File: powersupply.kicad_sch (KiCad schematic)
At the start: 24 parts, among them SW1 SW_SPST, U3 MP28167GQ, U4 1047

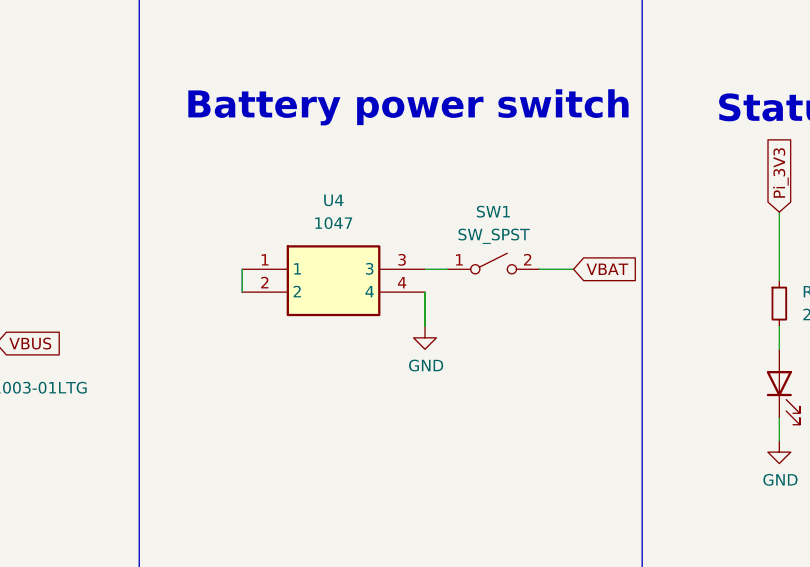
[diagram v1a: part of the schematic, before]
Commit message: Replace the switch with the real one: 633-CS12ANW03
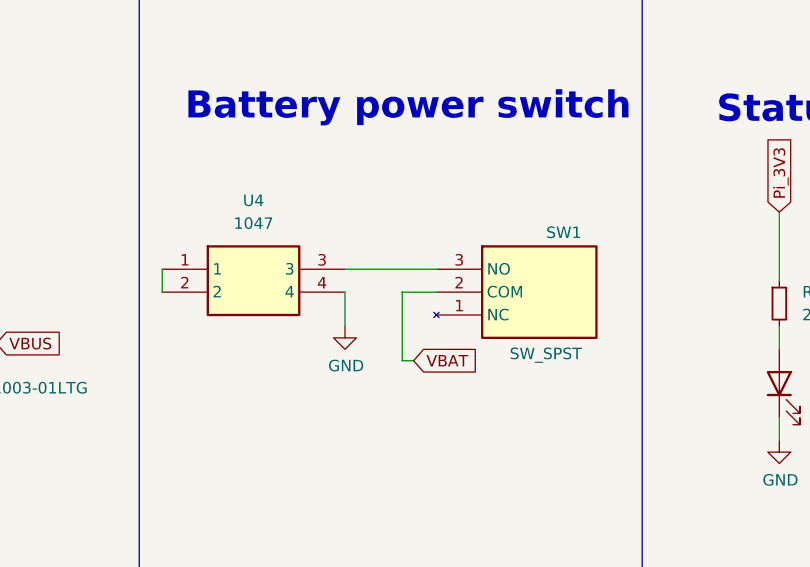
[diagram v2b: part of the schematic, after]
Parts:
- SW1: footprint Button_Switch_THT:SW_DIP_SPSTx01_Slide_9.78x4.72mm_W7.62mm_P2.54mm -> CS12ANW03; symbol Switch:SW_SPST -> STS1_EEE_lib:CS12ANW03; Height (none) -> 13.6; Manufacturer_Name (none) -> NKK Switches; Manufacturer_Part_Number (none) -> CS12ANW03; Mouser Part Number (none) -> 633-CS12ANW03; Mouser Price/Stock (none) -> https://www.mouser.co.uk/ProductDetail/NKK-Switches/CS12ANW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
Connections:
- net at SW1.1 (NC): no longer U4.3
- new net: SW1.3 (NO), U4.3
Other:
- moved on the sheet: U4
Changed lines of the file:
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@@
 	(wire
 		(pts
-			(xy 293.37 48.26) (xy 293.37 52.07)
+			(xy 284.48 48.26) (xy 284.48 52.07)
 		)
 		(stroke
@@
 	(wire
 		(pts
-			(xy 293.37 45.72) (xy 295.91 45.72)
+			(xy 284.48 45.72) (xy 294.64 45.72)
 		)
 		(stroke
@@
 	(wire
 		(pts
+			(xy 290.83 48.26) (xy 290.83 55.88)
+		)
+		(stroke
+			(width 0)
+			(type default)
+		)
+	)
+	(wire
+		(pts
 			(xy 344.17 39.37) (xy 344.17 46.99)
 		)
@@
 	(wire
 		(pts
-			(xy 273.05 45.72) (xy 273.05 48.26)
+			(xy 264.16 45.72) (xy 264.16 48.26)
 		)
 		(stroke
@@
 	(wire
 		(pts
-			(xy 306.07 45.72) (xy 309.88 45.72)
+			(xy 294.64 48.26) (xy 290.83 48.26)
 		)
 		(stroke
@@
 	(wire
 		(pts
+			(xy 290.83 55.88) (xy 292.1 55.88)
+		)
+		(stroke
+			(width 0)
+			(type default)
+		)
+	)
+	(wire
+		(pts
 			(xy 240.665 62.865) (xy 240.665 61.595)
 		)
@@
 	(global_label "VBAT"
 		(shape input)
-		(at 309.88 45.72 0)
+		(at 292.1 55.88 0)
 		(fields_autoplaced yes)
 		(effects
@@
 		)
 		(property "Intersheetrefs" "${INTERSHEET_REFS}"
-			(at 316.6258 45.72 0)
+			(at 298.8458 55.88 0)
 			(hide yes)
 			(show_name no)
@@
 	)
 	(symbol
-		(lib_id "Switch:SW_SPST")
-		(at 300.99 45.72 0)
+		(lib_id "STS1_EEE_lib:CS12ANW03")
+		(at 294.64 45.72 0)
 		(unit 1)
 		(body_style 1)
@@
 		(in_pos_files yes)
 		(dnp no)
-		(fields_autoplaced yes)
 		(property "Reference" "SW1"
-			(at 300.99 39.37 0)
+			(at 306.832 41.656 0)
 			(show_name no)
 			(do_not_autoplace no)
@@
 					(size 1.27 1.27)
 				)
+				(justify left)
 			)
 		)
 		(property "Value" "SW_SPST"
-			(at 300.99 41.91 0)
+			(at 302.768 55.118 0)
 			(show_name no)
 			(do_not_autoplace no)
@@
 					(size 1.27 1.27)
 				)
+				(justify left)
 			)
 		)
-		(property "Footprint" "Button_Switch_THT:SW_DIP_SPSTx01_Slide_9.78x4.72mm_W7.62mm_P2.54mm"
-			(at 300.99 45.72 0)
+		(property "Footprint" "CS12ANW03"
+			(at 313.69 140.64 0)
 			(hide yes)
 			(show_name no)
@@
 					(size 1.27 1.27)
 				)
+				(justify left top)
 			)
 		)
-		(property "Datasheet" ""
-			(at 300.99 45.72 0)
+		(property "Datasheet" "https://www.nkkswitches.com.hk/products/Slides/Slides%20CS/CS12ANW03/"
+			(at 313.69 240.64 0)
+			(hide yes)
+			(show_name no)
+			(do_not_autoplace no)
+			(effects
+				(font
+					(size 1.27 1.27)
+				)
+				(justify left top)
+			)
+		)
+		(property "Description" "NKK SWITCHES - CS12ANW03 - SWITCH, SLIDE, SPDT, 3A, 250V, TH"
+			(at 294.64 45.72 0)
+			(hide yes)
+			(show_name no)
+			(do_not_autoplace no)
+			(effects
+				(font
+					(size 1.27 1.27)
+				)
+			)
+		)
+		(property "Height" "13.6"
+			(at 313.69 440.64 0)
 			(hide yes)
 			(show_name no)
@@
 					(size 1.27 1.27)
 				)
+				(justify left top)
 			)
 		)
-		(property "Description" "Single Pole Single Throw (SPST) switch"
-			(at 300.99 45.72 0)
+		(property "Mouser Part Number" "633-CS12ANW03"
+			(at 313.69 540.64 0)
 			(hide yes)
 			(show_name no)
@@
 					(size 1.27 1.27)
 				)
+				(justify left top)
+			)
+		)
+		(property "Mouser Price/Stock" "https://www.mouser.co.uk/ProductDetail/NKK-Switches/CS12ANW03?qs=4P1McwaGddbVHu%252BBZT0egw%3D%3D"
+			(at 313.69 640.64 0)
+			(hide yes)
+			(show_name no)
+			(do_not_autoplace no)
+			(effects
+				(font
+					(size 1.27 1.27)
+				)
+				(justify left top)
+			)
+		)
+		(property "Manufacturer_Name" "NKK Switches"
+			(at 313.69 740.64 0)
+			(hide yes)
+			(show_name no)
+			(do_not_autoplace no)
+			(effects
+				(font
+					(size 1.27 1.27)
+				)
+				(justify left top)
+			)
+		)
+		(property "Manufacturer_Part_Number" "CS12ANW03"
+			(at 313.69 840.64 0)
+			(hide yes)
+			(show_name no)
+			(do_not_autoplace no)
+			(effects
+				(font
+					(size 1.27 1.27)
+				)
+				(justify left top)
 			)
 		)
@@
 		(pin "1"
 		)
+		(pin "3"
+		)
 		(instances
 			(project "STS1_EEE"
@@
 	(symbol
 		(lib_id "power:GND")
-		(at 293.37 52.07 0)
+		(at 284.48 52.07 0)
 		(unit 1)
 		(body_style 1)
@@
 		(dnp no)
 		(property "Reference" "#PWR047"
-			(at 293.37 58.42 0)
+			(at 284.48 58.42 0)
 			(hide yes)
 			(show_name no)
@@
 		)
 		(property "Value" "GND"
-			(at 293.497 56.4642 0)
+			(at 284.607 56.4642 0)
 			(show_name no)
 			(do_not_autoplace no)
@@
 		)
 		(property "Footprint" ""
-			(at 293.37 52.07 0)
+			(at 284.48 52.07 0)
 			(hide yes)
 			(show_name no)
@@
 		)
 		(property "Datasheet" ""
-			(at 293.37 52.07 0)
+			(at 284.48 52.07 0)
 			(hide yes)
 			(show_name no)
@@
 		)
 		(property "Description" "Power symbol creates a global label with name \"GND\" , ground"
-			(at 293.37 52.07 0)
+			(at 284.48 52.07 0)
 			(hide yes)
 			(show_name no)
@@
 	(symbol
 		(lib_id "STS1_EEE_lib:1048P")
-		(at 273.05 45.72 0)
+		(at 264.16 45.72 0)
 		(unit 1)
 		(body_style 1)
@@
 		(fields_autoplaced yes)
 		(property "Reference" "U4"
-			(at 283.21 38.1 0)
+			(at 274.32 38.1 0)
 			(show_name no)
 			(do_not_autoplace no)
@@
 		)
 		(property "Value" "1047"
-			(at 283.21 40.64 0)
+			(at 274.32 40.64 0)
 			(show_name no)
 			(do_not_autoplace no)
@@
 		)
 		(property "Footprint" "STS_EEE:1048P"
-			(at 289.56 140.64 0)
+			(at 280.67 140.64 0)
 			(hide yes)
 			(show_name no)
@@
 		)
 		(property "Datasheet" "http://www.keyelco.com/product-pdf.cfm?p=13959"
-			(at 289.56 240.64 0)
+			(at 280.67 240.64 0)
 			(hide yes)
 			(show_name no)
@@
 		)
 		(property "Description" "KEYSTONE - 1048P - BATTERY HOLDER, 18650, SMD"
-			(at 273.05 45.72 0)
+			(at 264.16 45.72 0)
 			(hide yes)
 			(show_name no)
@@
 		)
 		(property "Height" "14.85"
-			(at 289.56 440.64 0)
+			(at 280.67 440.64 0)
 			(hide yes)
 			(show_name no)
@@
 		)
 		(property "Mouser Part Number" "534-1048P"
-			(at 289.56 540.64 0)
+			(at 280.67 540.64 0)
 			(hide yes)
 			(show_name no)
@@
 		)
 		(property "Mouser Price/Stock" "https://www.mouser.co.uk/ProductDetail/Keystone-Electronics/1048P?qs=9%252Bwcgl%2FJqd1h8Vx3IFpTxA%3D%3D"
-			(at 289.56 640.64 0)
+			(at 280.67 640.64 0)
 			(hide yes)
 			(show_name no)
@@
 		)
 		(property "Manufacturer_Name" "Keystone Electronics"
-			(at 289.56 740.64 0)
+			(at 280.67 740.64 0)
 			(hide yes)
 			(show_name no)
@@
 		)
 		(property "Manufacturer_Part_Number" "1048P"
-			(at 289.56 840.64 0)
+			(at 280.67 840.64 0)
 			(hide yes)
 			(show_name no)

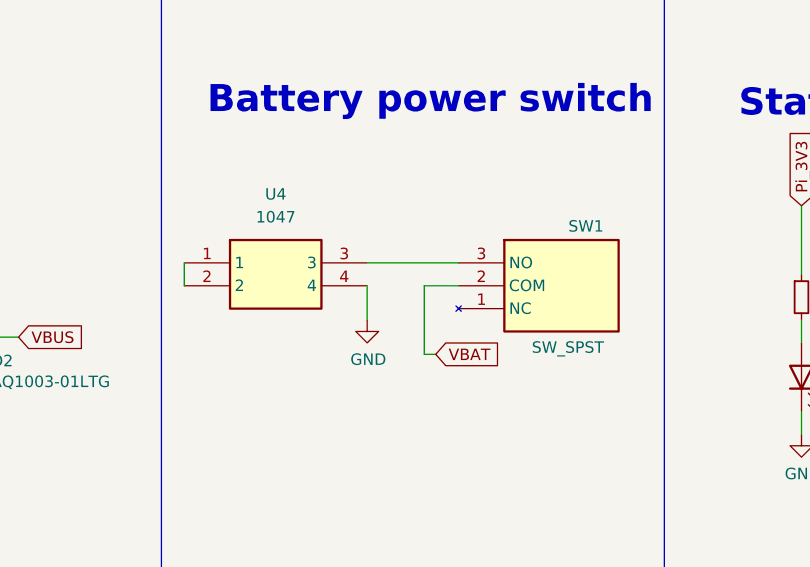
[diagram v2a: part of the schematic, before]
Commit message: Replace batter holder: 1048P -> 1049
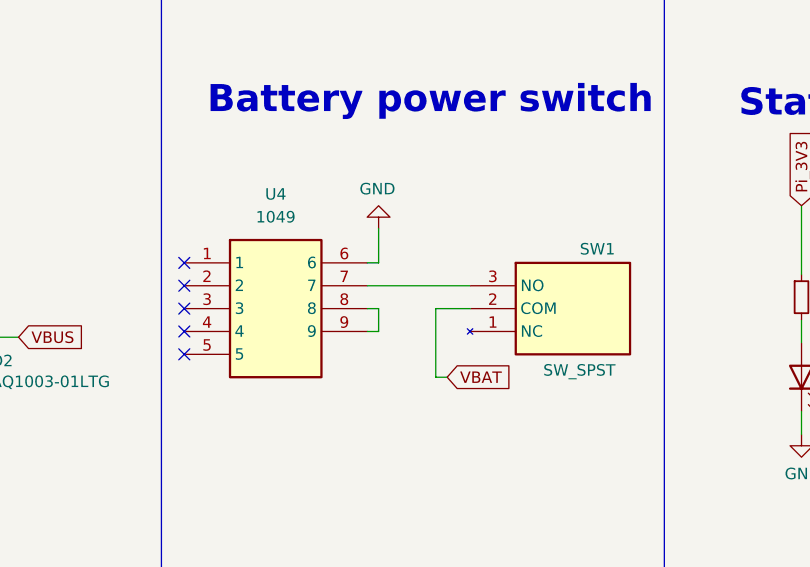
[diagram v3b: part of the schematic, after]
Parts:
- U4: value 1047 -> 1049; footprint STS_EEE:1048P -> 1049; symbol STS1_EEE_lib:1048P -> STS1_EEE_lib:1049; Height 14.85 -> 14; Manufacturer_Part_Number 1048P -> 1049; Mouser Part Number 534-1048P -> 534-1049; Mouser Price/Stock https://www.mouser.co.uk/ProductDetail/Keystone-Electronics/1048P?qs=9%252Bwcgl%2FJqd1h8Vx3IFpTxA%3D%3D -> https://www.mouser.co.uk/ProductDetail/Keystone-Electronics/1049?qs=%2F7TOpeL5Mz78b0pqEFIl5w%3D%3D
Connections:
- net AGND: now also U4.6; no longer U4.4
- net at SW1.3 (NO): now also U4.7; no longer U4.3
- net at U4.1: no longer U4.2
- new net: U4.8, U4.9
- no-connect marks 0 -> 5
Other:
- moved on the sheet: SW1
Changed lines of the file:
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@@
 		(color 0 0 0 0)
 	)
+	(no_connect
+		(at 264.16 50.8)
+	)
+	(no_connect
+		(at 264.16 55.88)
+	)
+	(no_connect
+		(at 264.16 45.72)
+	)
+	(no_connect
+		(at 264.16 53.34)
+	)
+	(no_connect
+		(at 264.16 48.26)
+	)
+	(wire
+		(pts
+			(xy 284.48 45.72) (xy 285.75 45.72)
+		)
+		(stroke
+			(width 0)
+			(type default)
+		)
+	)
 	(wire
 		(pts
@@
 	(wire
 		(pts
-			(xy 94.615 48.895) (xy 94.615 47.625)
+			(xy 284.48 48.26) (xy 295.91 48.26)
 		)
 		(stroke
@@
 	(wire
 		(pts
-			(xy 332.74 62.23) (xy 332.74 64.77)
+			(xy 94.615 48.895) (xy 94.615 47.625)
 		)
 		(stroke
@@
 	(wire
 		(pts
-			(xy 193.675 42.545) (xy 193.675 37.465)
+			(xy 332.74 62.23) (xy 332.74 64.77)
 		)
 		(stroke
@@
 	(wire
 		(pts
-			(xy 227.965 53.975) (xy 240.665 53.975)
+			(xy 193.675 42.545) (xy 193.675 37.465)
 		)
 		(stroke
@@
 	(wire
 		(pts
-			(xy 284.48 48.26) (xy 284.48 52.07)
+			(xy 227.965 53.975) (xy 240.665 53.975)
 		)
 		(stroke
@@
 	(wire
 		(pts
-			(xy 284.48 45.72) (xy 294.64 45.72)
-		)
-		(stroke
-			(width 0)
-			(type default)
-		)
-	)
-	(wire
-		(pts
 			(xy 120.015 76.835) (xy 120.015 75.565)
 		)
@@
 	(wire
 		(pts
-			(xy 290.83 48.26) (xy 290.83 55.88)
+			(xy 292.1 50.8) (xy 292.1 58.42)
 		)
 		(stroke
@@
 	(wire
 		(pts
+			(xy 285.75 41.91) (xy 285.75 45.72)
+		)
+		(stroke
+			(width 0)
+			(type default)
+		)
+	)
+	(wire
+		(pts
 			(xy 120.015 46.355) (xy 130.175 46.355)
 		)
@@
 	(wire
 		(pts
+			(xy 284.48 50.8) (xy 285.75 50.8)
+		)
+		(stroke
+			(width 0)
+			(type default)
+		)
+	)
+	(wire
+		(pts
 			(xy 170.815 62.865) (xy 170.815 71.755)
 		)
@@
 	(wire
 		(pts
-			(xy 264.16 45.72) (xy 264.16 48.26)
+			(xy 284.48 53.34) (xy 285.75 53.34)
 		)
 		(stroke
@@
 	(wire
 		(pts
-			(xy 294.64 48.26) (xy 290.83 48.26)
+			(xy 295.91 50.8) (xy 292.1 50.8)
 		)
 		(stroke
@@
 	(wire
 		(pts
-			(xy 290.83 55.88) (xy 292.1 55.88)
+			(xy 292.1 58.42) (xy 293.37 58.42)
+		)
+		(stroke
+			(width 0)
+			(type default)
+		)
+	)
+	(wire
+		(pts
+			(xy 285.75 50.8) (xy 285.75 53.34)
 		)
 		(stroke
@@
 	(global_label "VBAT"
 		(shape input)
-		(at 292.1 55.88 0)
+		(at 293.37 58.42 0)
 		(fields_autoplaced yes)
 		(effects
@@
 		)
 		(property "Intersheetrefs" "${INTERSHEET_REFS}"
-			(at 298.8458 55.88 0)
+			(at 300.1158 58.42 0)
 			(hide yes)
 			(show_name no)
@@
 	(symbol
 		(lib_id "STS1_EEE_lib:CS12ANW03")
-		(at 294.64 45.72 0)
+		(at 295.91 48.26 0)
 		(unit 1)
 		(body_style 1)
@@
 		(dnp no)
 		(property "Reference" "SW1"
-			(at 306.832 41.656 0)
+			(at 308.102 44.196 0)
 			(show_name no)
 			(do_not_autoplace no)
@@
 		)
 		(property "Value" "SW_SPST"
-			(at 302.768 55.118 0)
+			(at 304.038 57.658 0)
 			(show_name no)
 			(do_not_autoplace no)
@@
 		)
 		(property "Footprint" "CS12ANW03"
-			(at 313.69 140.64 0)
+			(at 314.96 143.18 0)
 			(hide yes)
 			(show_name no)
@@
 		)
 		(property "Datasheet" "https://www.nkkswitches.com.hk/products/Slides/Slides%20CS/CS12ANW03/"
-			(at 313.69 240.64 0)
+			(at 314.96 243.18 0)
 			(hide yes)
 			(show_name no)
@@
 		)
 		(property "Description" "NKK SWITCHES - CS12ANW03 - SWITCH, SLIDE, SPDT, 3A, 250V, TH"
-			(at 294.64 45.72 0)
+			(at 295.91 48.26 0)
 			(hide yes)
 			(show_name no)
@@
 		)
 		(property "Height" "13.6"
-			(at 313.69 440.64 0)
+			(at 314.96 443.18 0)
 			(hide yes)
 			(show_name no)
@@
 		)
 		(property "Mouser Part Number" "633-CS12ANW03"
-			(at 313.69 540.64 0)
+			(at 314.96 543.18 0)
 			(hide yes)
 			(show_name no)
@@
 		)
 		(property "Mouser Price/Stock" "https://www.mouser.co.uk/ProductDetail/NKK-Switches/CS12ANW03?qs=4P1McwaGddbVHu%252BBZT0egw%3D%3D"
-			(at 313.69 640.64 0)
+			(at 314.96 643.18 0)
 			(hide yes)
 			(show_name no)
@@
 		)
 		(property "Manufacturer_Name" "NKK Switches"
-			(at 313.69 740.64 0)
+			(at 314.96 743.18 0)
 			(hide yes)
 			(show_name no)
@@
 		)
 		(property "Manufacturer_Part_Number" "CS12ANW03"
-			(at 313.69 840.64 0)
+			(at 314.96 843.18 0)
 			(hide yes)
 			(show_name no)
@@
 	(symbol
 		(lib_id "power:GND")
-		(at 284.48 52.07 0)
+		(at 285.75 41.91 180)
 		(unit 1)
 		(body_style 1)
@@
 		(dnp no)
 		(property "Reference" "#PWR047"
-			(at 284.48 58.42 0)
+			(at 285.75 35.56 0)
 			(hide yes)
 			(show_name no)
@@
 		)
 		(property "Value" "GND"
-			(at 284.607 56.4642 0)
+			(at 285.623 37.5158 0)
 			(show_name no)
 			(do_not_autoplace no)
@@
 		)
 		(property "Footprint" ""
-			(at 284.48 52.07 0)
+			(at 285.75 41.91 0)
 			(hide yes)
 			(show_name no)
@@
 		)
 		(property "Datasheet" ""
-			(at 284.48 52.07 0)
+			(at 285.75 41.91 0)
 			(hide yes)
 			(show_name no)
@@
 		)
 		(property "Description" "Power symbol creates a global label with name \"GND\" , ground"
-			(at 284.48 52.07 0)
+			(at 285.75 41.91 0)
 			(hide yes)
 			(show_name no)
@@
 	)
 	(symbol
-		(lib_id "STS1_EEE_lib:1048P")
+		(lib_id "STS1_EEE_lib:1049")
 		(at 264.16 45.72 0)
 		(unit 1)
@@
 			)
 		)
-		(property "Value" "1047"
+		(property "Value" "1049"
 			(at 274.32 40.64 0)
 			(show_name no)
@@
 			)
 		)
-		(property "Footprint" "STS_EEE:1048P"
+		(property "Footprint" "1049"
 			(at 280.67 140.64 0)
 			(hide yes)
@@
 			)
 		)
-		(property "Datasheet" "http://www.keyelco.com/product-pdf.cfm?p=13959"
+		(property "Datasheet" "http://www.keyelco.com/product.cfm/product_id/921"
 			(at 280.67 240.64 0)
 			(hide yes)
@@
 			)
 		)
-		(property "Description" "KEYSTONE - 1048P - BATTERY HOLDER, 18650, SMD"
+		(property "Description" "KEYSTONE - 1049 - BATTERY HOLDER, 18650, THROUGH HOLE"
 			(at 264.16 45.72 0)
 			(hide yes)
@@
 			)
 		)
-		(property "Height" "14.85"
+		(property "Height" "14"
 			(at 280.67 440.64 0)
 			(hide yes)
@@
 			)
 		)
-		(property "Mouser Part Number" "534-1048P"
+		(property "Mouser Part Number" "534-1049"
 			(at 280.67 540.64 0)
 			(hide yes)
@@
 			)
 		)
-		(property "Mouser Price/Stock" "https://www.mouser.co.uk/ProductDetail/Keystone-Electronics/1048P?qs=9%252Bwcgl%2FJqd1h8Vx3IFpTxA%3D%3D"
+		(property "Mouser Price/Stock" "https://www.mouser.co.uk/ProductDetail/Keystone-Electronics/1049?qs=%2F7TOpeL5Mz78b0pqEFIl5w%3D%3D"
 			(at 280.67 640.64 0)
 			(hide yes)
@@
 			)
 		)
-		(property "Manufacturer_Part_Number" "1048P"
+		(property "Manufacturer_Part_Number" "1049"
 			(at 280.67 840.64 0)
 			(hide yes)
@@
 		(pin "1"
 		)
+		(pin "9"
+		)
+		(pin "8"
+		)
+		(pin "7"
+		)
+		(pin "6"
+		)
+		(pin "5"
+		)
 		(instances
